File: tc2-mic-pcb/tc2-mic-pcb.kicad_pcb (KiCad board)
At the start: 2 copper layers, 39 x 12 mm, 14 parts, among them J1 Screw_Terminal_01x01, J2 Screw_Terminal_01x01, J4 Conn_02x03_Odd_Even, U2 TXS0102DCT, U3 AP7335-18SNG-7

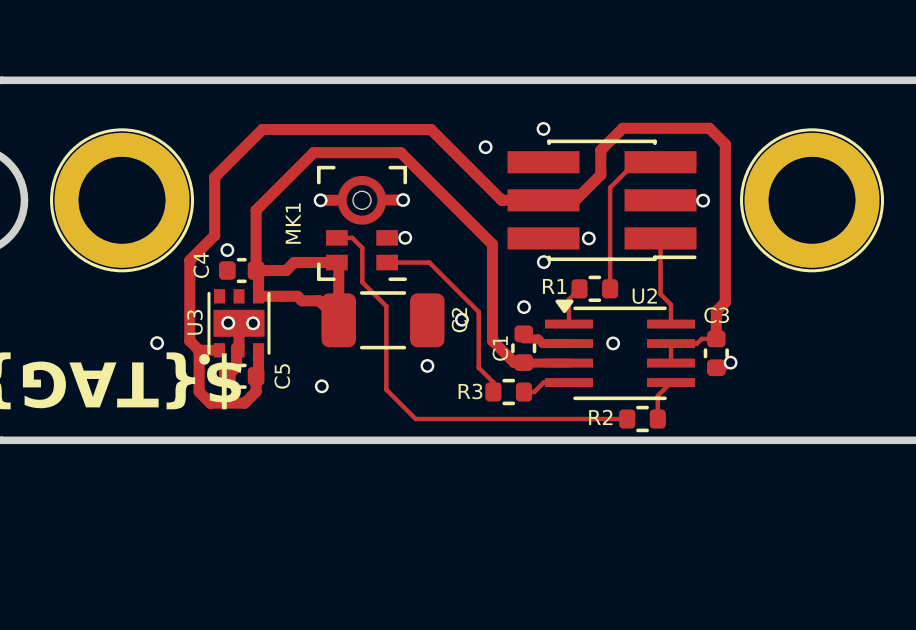
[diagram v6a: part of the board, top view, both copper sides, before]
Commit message: Update to use touch sensor
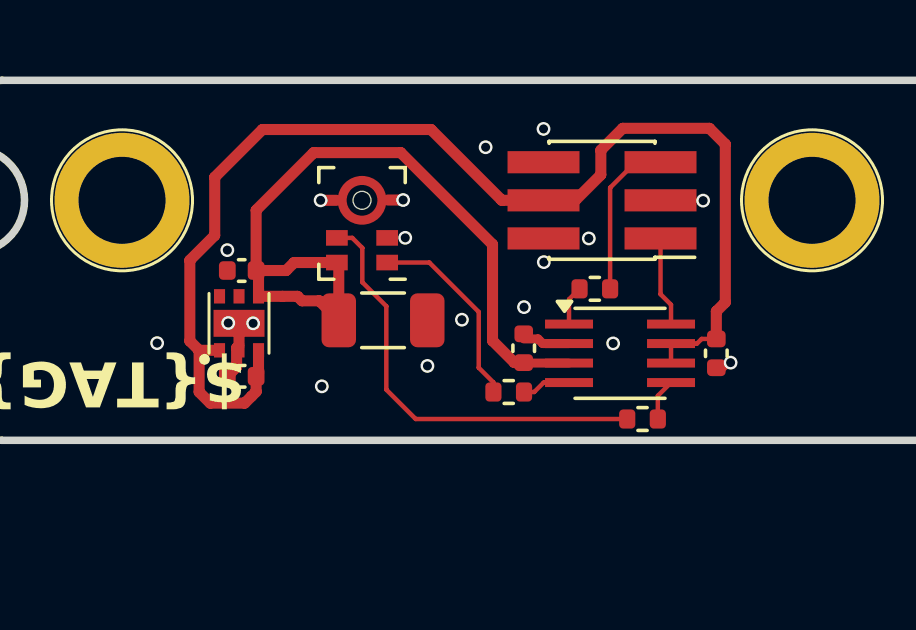
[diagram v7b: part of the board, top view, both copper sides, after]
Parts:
- renumbered C1 to C401, C3 to C402, C2 to C403, C5 to C404, C4 to C405, J4 to J401, J2 to J402, J1 to J403, MK1 to MK401, R2 to R401, R3 to R402, R1 to R403, U3 to U401, U2 to U402
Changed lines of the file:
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@@
 	(net 4 "+3V3")
 	(net 5 "PDM_DATA")
-	(net 6 "unconnected-(U3-NC-Pad5)")
-	(net 7 "unconnected-(U3-NC{slash}ADJ-Pad6)")
+	(net 6 "unconnected-(J402-Pin_1-Pad1)")
+	(net 7 "unconnected-(J403-Pin_1-Pad1)")
 	(net 8 "/DATA_PHY")
 	(net 9 "/CLOCK")
@@
 	(net 11 "/DATA")
 	(net 12 "/CLOCK_PHY")
-	(net 13 "unconnected-(J1-Pin_1-Pad1)")
-	(net 14 "unconnected-(J2-Pin_1-Pad1)")
+	(net 13 "unconnected-(U401-NC{slash}ADJ-Pad6)")
+	(net 14 "unconnected-(U401-NC-Pad5)")
 	(footprint "Connector_PinHeader_1.27mm:PinHeader_2x03_P1.27mm_Vertical_SMD"
 		(layer "F.Cu")
@@
 		(descr "surface-mounted straight pin header, 2x03, 1.27mm pitch, double rows")
 		(tags "Surface mounted pin header SMD 2x03 1.27mm double row")
-		(property "Reference" "J4"
+		(property "Reference" "J401"
 			(at 0 -2.965 0)
 			(layer "F.SilkS")
@@
 				(font
 					(size 1.27 1.27)
+					(thickness 0.15)
 				)
 			)
@@
 				(font
 					(size 1.27 1.27)
+					(thickness 0.15)
 				)
 			)
@@
 				(font
 					(size 1.27 1.27)
+					(thickness 0.15)
 				)
 			)
@@
 		(layer "F.Cu")
 		(at 23 0)
-		(property "Reference" "J1"
+		(property "Reference" "J403"
 			(at 0 -3.2 0)
 			(layer "F.SilkS")
@@
 				(font
 					(size 1.27 1.27)
+					(thickness 0.15)
 				)
 			)
@@
 				(font
 					(size 1.27 1.27)
+					(thickness 0.15)
 				)
 			)
@@
 				(font
 					(size 1.27 1.27)
+					(thickness 0.15)
 				)
 			)
@@
 			(layers "*.Cu" "*.Mask")
 			(remove_unused_layers no)
-			(net 13 "unconnected-(J1-Pin_1-Pad1)")
+			(net 7 "unconnected-(J403-Pin_1-Pad1)")
 			(pinfunction "Pin_1")
 			(pintype "passive+no_connect")
@@
 		(descr "SSOP-8 2.9 x2.8mm Pitch 0.65mm")
 		(tags "SSOP-8 2.95x2.8mm Pitch 0.65mm")
-		(property "Reference" "U2"
+		(property "Reference" "U402"
 			(at 0.83 -1.89 0)
 			(layer "F.SilkS")
+			(hide yes)
 			(effects
 				(font
@@
 				(font
 					(size 1.27 1.27)
+					(thickness 0.15)
 				)
 			)
@@
 				(font
 					(size 1.27 1.27)
+					(thickness 0.15)
 				)
 			)
@@
 				(font
 					(size 1.27 1.27)
+					(thickness 0.15)
 				)
 			)
@@
 		(layer "F.Cu")
 		(at 3.9 4.1)
-		(property "Reference" "U3"
+		(property "Reference" "U401"
 			(at -1.45 -0.03 90)
 			(layer "F.SilkS")
+			(hide yes)
 			(effects
 				(font
@@
 				(font
 					(size 1.27 1.27)
+					(thickness 0.15)
 				)
 			)
@@
 				(font
 					(size 1.27 1.27)
+					(thickness 0.15)
 				)
 			)
@@
 				(font
 					(size 1.27 1.27)
+					(thickness 0.15)
 				)
 			)
@@
 			(size 0.37 0.48)
 			(layers "F.Cu" "F.Paste" "F.Mask")
-			(net 6 "unconnected-(U3-NC-Pad5)")
+			(net 14 "unconnected-(U401-NC-Pad5)")
 			(pinfunction "NC")
 			(pintype "unspecified+no_connect")
@@
 			(size 0.37 0.48)
 			(layers "F.Cu" "F.Paste" "F.Mask")
-			(net 7 "unconnected-(U3-NC{slash}ADJ-Pad6)")
+			(net 13 "unconnected-(U401-NC{slash}ADJ-Pad6)")
 			(pinfunction "NC/ADJ")
 			(pintype "unspecified+no_connect")
@@
 		(descr "Capacitor SMD 0402 (1005 Metric), square (rectangular) end terminal, IPC_7351 nominal, (Body size source: IPC-SM-782 page 76, https://www.pcb-3d.com/wordpress/wp-content/uploads/ipc-sm-782a_amendment_1_and_2.pdf), generated with kicad-footprint-generator")
 		(tags "capacitor")
-		(property "Reference" "C1"
+		(property "Reference" "C401"
 			(at 0 -0.76 90)
 			(layer "F.SilkS")
+			(hide yes)
 			(effects
 				(font
@@
 				(font
 					(size 1.27 1.27)
+					(thickness 0.15)
 				)
 			)
@@
 				(font
 					(size 1.27 1.27)
+					(thickness 0.15)
 				)
 			)
@@
 				(font
 					(size 1.27 1.27)
+					(thickness 0.15)
 				)
 			)
@@
 		(descr "Capacitor SMD 1206 (3216 Metric), square (rectangular) end terminal, IPC_7351 nominal, (Body size source: IPC-SM-782 page 76, https://www.pcb-3d.com/wordpress/wp-content/uploads/ipc-sm-782a_amendment_1_and_2.pdf), generated with kicad-footprint-generator")
 		(tags "capacitor")
-		(property "Reference" "C2"
+		(property "Reference" "C403"
 			(at 2.57 -0.02 90)
 			(layer "F.SilkS")
+			(hide yes)
 			(effects
 				(font
@@
 				(font
 					(size 1.27 1.27)
+					(thickness 0.15)
 				)
 			)
@@
 				(font
 					(size 1.27 1.27)
+					(thickness 0.15)
 				)
 			)
@@
 				(font
 					(size 1.27 1.27)
+					(thickness 0.15)
 				)
 			)
@@
 		(layer "F.Cu")
 		(at 0 0)
-		(property "Reference" "J2"
+		(property "Reference" "J402"
 			(at 0 -3.2 0)
 			(layer "F.SilkS")
@@
 				(font
 					(size 1.27 1.27)
+					(thickness 0.15)
 				)
 			)
@@
 				(font
 					(size 1.27 1.27)
+					(thickness 0.15)
 				)
 			)
@@
 				(font
 					(size 1.27 1.27)
+					(thickness 0.15)
 				)
 			)
@@
 			(layers "*.Cu" "*.Mask")
 			(remove_unused_layers no)
-			(net 14 "unconnected-(J2-Pin_1-Pad1)")
+			(net 6 "unconnected-(J402-Pin_1-Pad1)")
 			(pinfunction "Pin_1")
 			(pintype "passive+no_connect")
@@
 		(descr "Resistor SMD 0402 (1005 Metric), square (rectangular) end terminal, IPC_7351 nominal, (Body size source: IPC-SM-782 page 72, https://www.pcb-3d.com/wordpress/wp-content/uploads/ipc-sm-782a_amendment_1_and_2.pdf), generated with kicad-footprint-generator")
 		(tags "resistor")
-		(property "Reference" "R1"
+		(property "Reference" "R403"
 			(at -1.34 -0.06 0)
 			(layer "F.SilkS")
+			(hide yes)
 			(effects
 				(font
@@
 				(font
 					(size 1.27 1.27)
+					(thickness 0.15)
 				)
 			)
@@
 				(font
 					(size 1.27 1.27)
+					(thickness 0.15)
 				)
 			)
@@
 				(font
 					(size 1.27 1.27)
+					(thickness 0.15)
 				)
 			)
@@
 		(descr "Capacitor SMD 0402 (1005 Metric), square (rectangular) end terminal, IPC_7351 nominal, (Body size source: IPC-SM-782 page 76, https://www.pcb-3d.com/wordpress/wp-content/uploads/ipc-sm-782a_amendment_1_and_2.pdf), generated with kicad-footprint-generator")
 		(tags "capacitor")
-		(property "Reference" "C5"
+		(property "Reference" "C404"
 			(at -1.37 0.005 90)
 			(layer "F.SilkS")
+			(hide yes)
 			(effects
 				(font
@@
 				(font
 					(size 1.27 1.27)
+					(thickness 0.15)
 				)
 			)
@@
 				(font
 					(size 1.27 1.27)
+					(thickness 0.15)
 				)
 			)
@@
 				(font
 					(size 1.27 1.27)
+					(thickness 0.15)
 				)
 			)
@@
 		(descr "Resistor SMD 0402 (1005 Metric), square (rectangular) end terminal, IPC_7351 nominal, (Body size source: IPC-SM-782 page 72, https://www.pcb-3d.com/wordpress/wp-content/uploads/ipc-sm-782a_amendment_1_and_2.pdf), generated with kicad-footprint-generator")
 		(tags "resistor")
-		(property "Reference" "R3"
+		(property "Reference" "R402"
 			(at -1.28 0 0)
 			(layer "F.SilkS")
+			(hide yes)
 			(effects
 				(font
@@
 				(font
 					(size 1.27 1.27)
+					(thickness 0.15)
 				)
 			)
@@
 				(font
 					(size 1.27 1.27)
+					(thickness 0.15)
 				)
 			)
@@
 				(font
 					(size 1.27 1.27)
+					(thickness 0.15)
 				)
 			)
@@
 		(descr "Capacitor SMD 0402 (1005 Metric), square (rectangular) end terminal, IPC_7351 nominal, (Body size source: IPC-SM-782 page 76, https://www.pcb-3d.com/wordpress/wp-content/uploads/ipc-sm-782a_amendment_1_and_2.pdf), generated with kicad-footprint-generator")
 		(tags "capacitor")
-		(property "Reference" "C3"
+		(property "Reference" "C402"
 			(at -1.25 -0.02 0)
 			(layer "F.SilkS")
+			(hide yes)
 			(effects
 				(font
@@
 				(font
 					(size 1.27 1.27)
+					(thickness 0.15)
 				)
 			)
@@
 				(font
 					(size 1.27 1.27)
+					(thickness 0.15)
 				)
 			)
@@
 				(font
 					(size 1.27 1.27)
+					(thickness 0.15)
 				)
 			)
@@
 		(descr "Resistor SMD 0402 (1005 Metric), square (rectangular) end terminal, IPC_7351 nominal, (Body size source: IPC-SM-782 page 72, https://www.pcb-3d.com/wordpress/wp-content/uploads/ipc-sm-782a_amendment_1_and_2.pdf), generated with kicad-footprint-generator")
 		(tags "resistor")
-		(property "Reference" "R2"
+		(property "Reference" "R401"
 			(at -1.39 -0.03 0)
 			(layer "F.SilkS")
+			(hide yes)
 			(effects
 				(font
@@
 				(font
 					(size 1.27 1.27)
+					(thickness 0.15)
 				)
 			)
@@
 				(font
 					(size 1.27 1.27)
+					(thickness 0.15)
 				)
 			)
@@
 				(font
 					(size 1.27 1.27)
+					(thickness 0.15)
 				)
 			)
@@
 		(descr "Capacitor SMD 0402 (1005 Metric), square (rectangular) end terminal, IPC_7351 nominal, (Body size source: IPC-SM-782 page 76, https://www.pcb-3d.com/wordpress/wp-content/uploads/ipc-sm-782a_amendment_1_and_2.pdf), generated with kicad-footprint-generator")
 		(tags "capacitor")
-		(property "Reference" "C4"
+		(property "Reference" "C405"
 			(at 1.33 0.17 90)
 			(layer "F.SilkS")
+			(hide yes)
 			(effects
 				(font
@@
 				(font
 					(size 1.27 1.27)
+					(thickness 0.15)
 				)
 			)
@@
 				(font
 					(size 1.27 1.27)
+					(thickness 0.15)
 				)
 			)
@@
 				(font
 					(size 1.27 1.27)
+					(thickness 0.15)
 				)
 			)
@@
 		(descr "https://www.knowles.com/docs/default-source/model-downloads/sph0641lu4h-1-revb.pdf")
 		(tags "MEMS Microphone LGA")
-		(property "Reference" "MK1"
+		(property "Reference" "MK401"
 			(at 2.2755 -0.008 90)
 			(layer "F.SilkS")
+			(hide yes)
 			(effects
 				(font
@@
 				(font
 					(size 1.27 1.27)
+					(thickness 0.15)
 				)
 			)
@@
 				(font
 					(size 1.27 1.27)
+					(thickness 0.15)
 				)
 			)
@@
 				(font
 					(size 1.27 1.27)
-				)
-			)
+					(thickness 0.15)
+				)
+			)

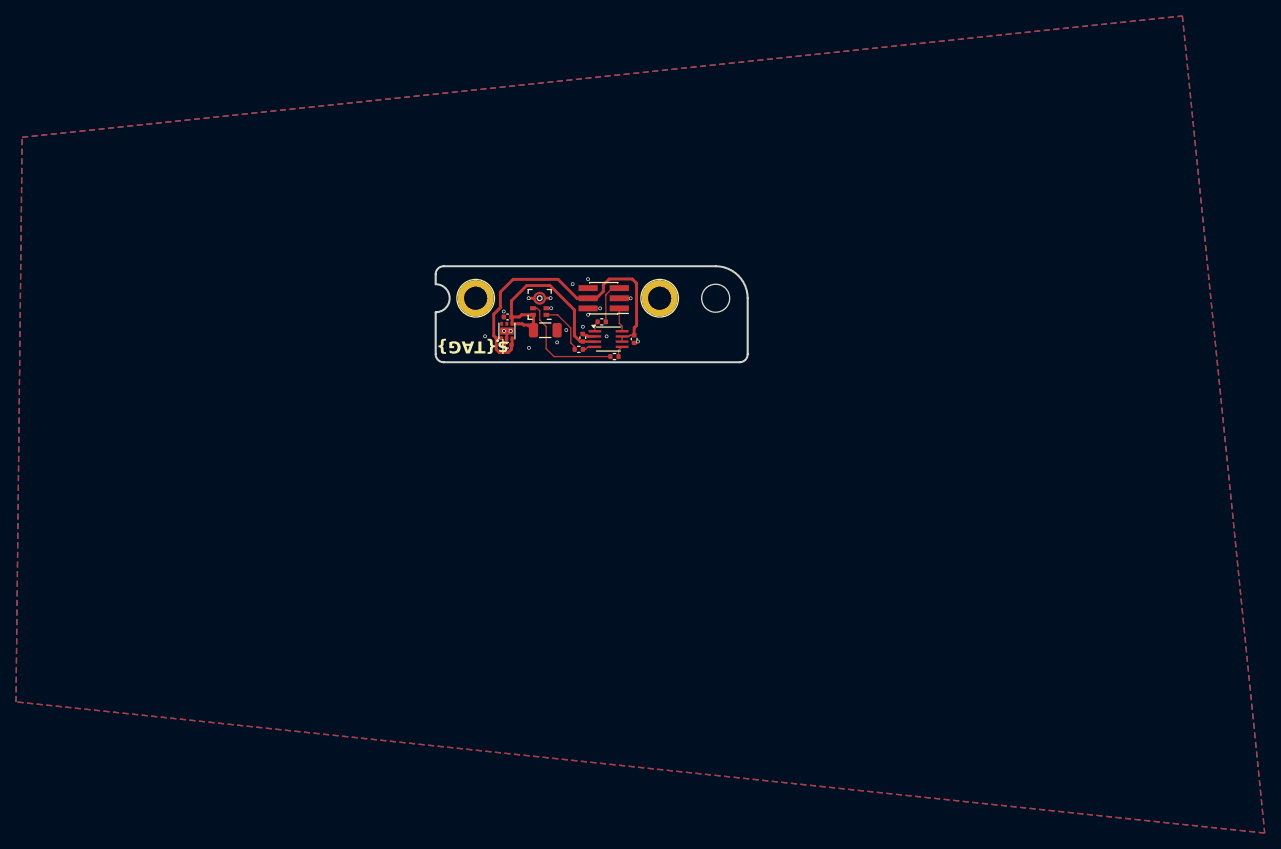
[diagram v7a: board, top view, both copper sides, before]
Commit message: v0.7.2 panelise microphone boards
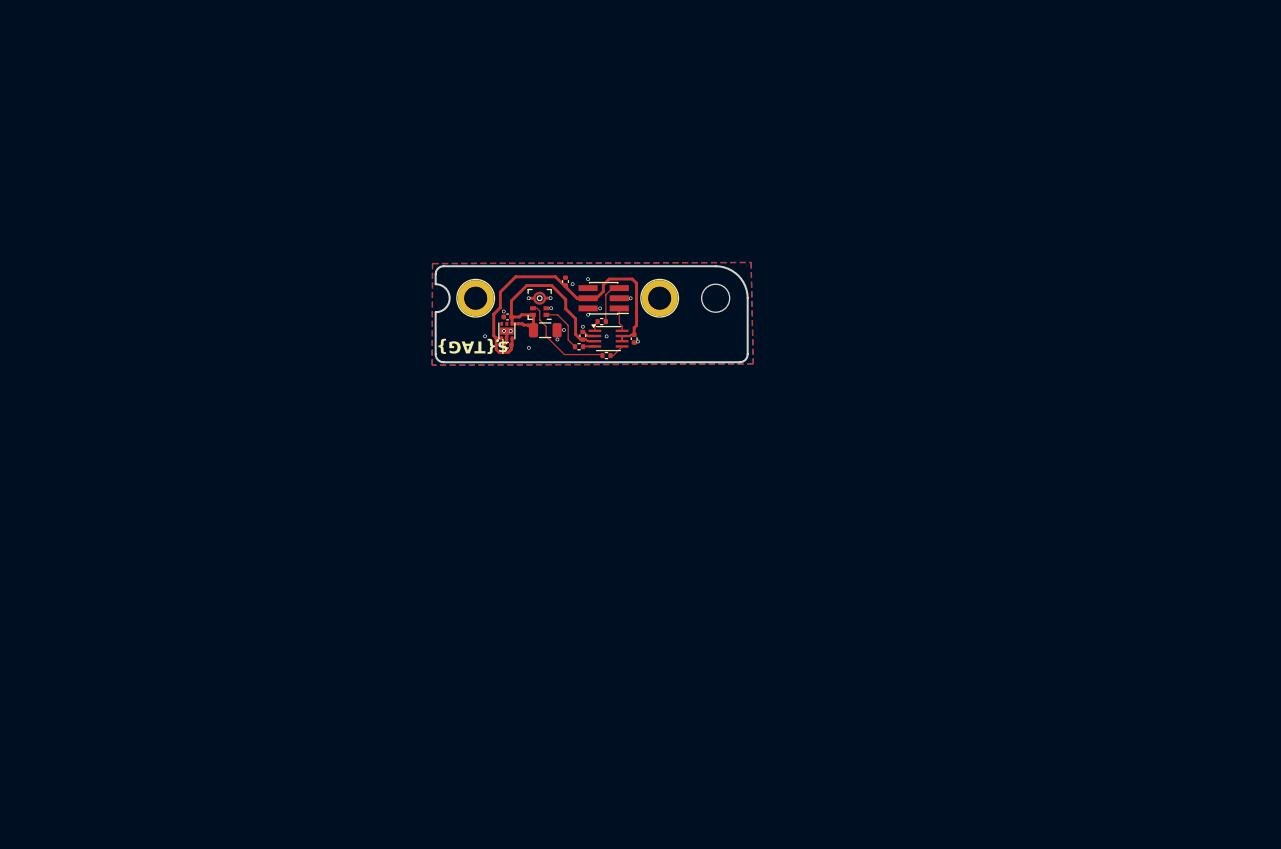
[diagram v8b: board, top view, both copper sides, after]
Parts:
- added C406: 1uF, Capacitor_SMD:C_0402_1005Metric, F.Cu at (11.2, -2.09)
- added REF**: Tab, PCM_kikit:Tab, F.Cu at (-5.44, 4.38)
- added REF**: Tab, PCM_kikit:Tab, F.Cu at (13.0, -4.40)
- added REF**: Tab, PCM_kikit:Tab, F.Cu at (13.0, 8.80)
- added REF**: Tab, PCM_kikit:Tab, F.Cu at (34.8, 4.38)
- moved R401 1.01 mm to (16.4, 7.17)
- moved R402 0.33 mm to (12.9, 6.06)
- moved C401 0.25 mm to (13.4, 4.68)
- moved C402 0.05 mm to (19.8, 5.05)
- moved U402 0.05 mm to (16.6, 5.05)
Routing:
- net /CLOCK: track 14.5 -> 12.5 mm
